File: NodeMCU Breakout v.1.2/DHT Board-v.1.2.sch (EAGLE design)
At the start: 12 parts, among them IC1 74HCT125N

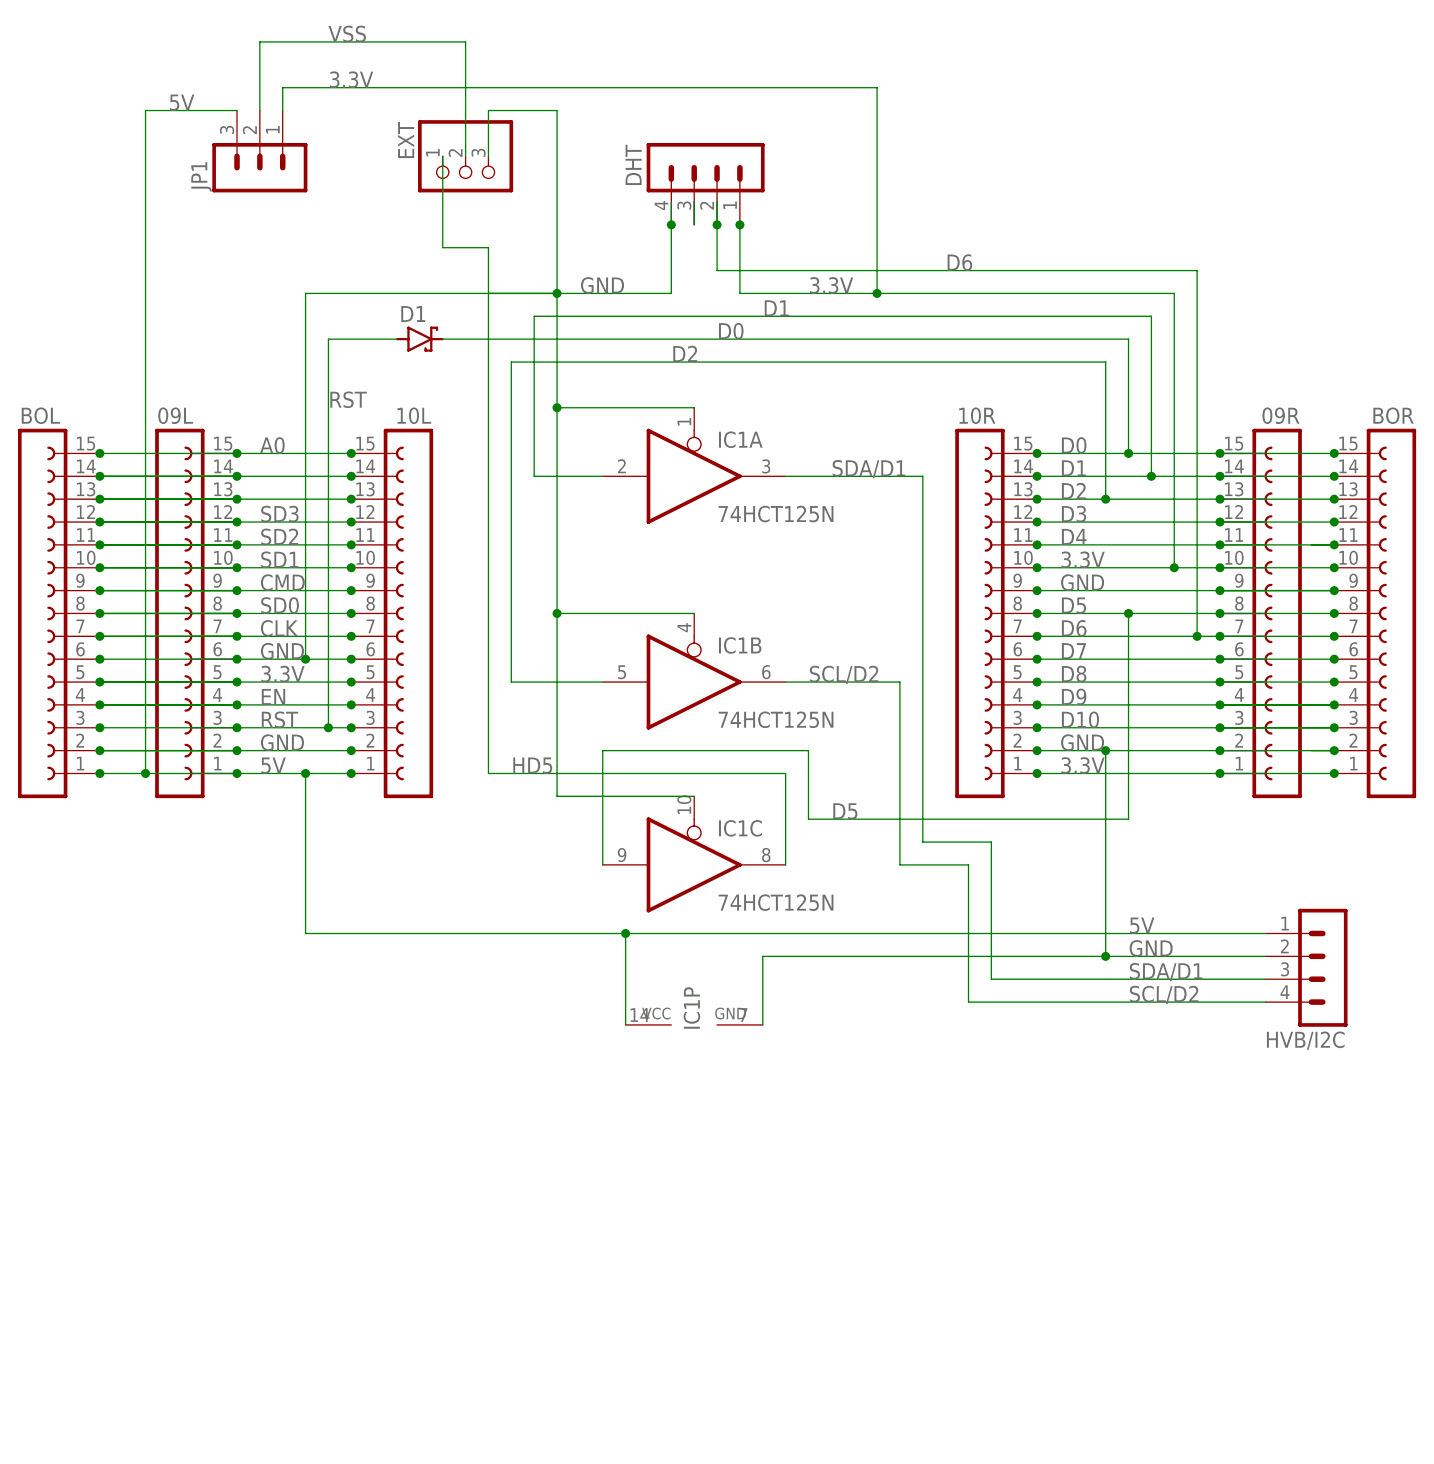
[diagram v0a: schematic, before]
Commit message: 12/26/18(BK): Updated with changes to EXT signal (D4, to make it compatible with all LED drivers), adding another pin to the I2C/HVB header, and adding a set of solder jumpers on the back of the board, for bypassing the level shifter as necessary.
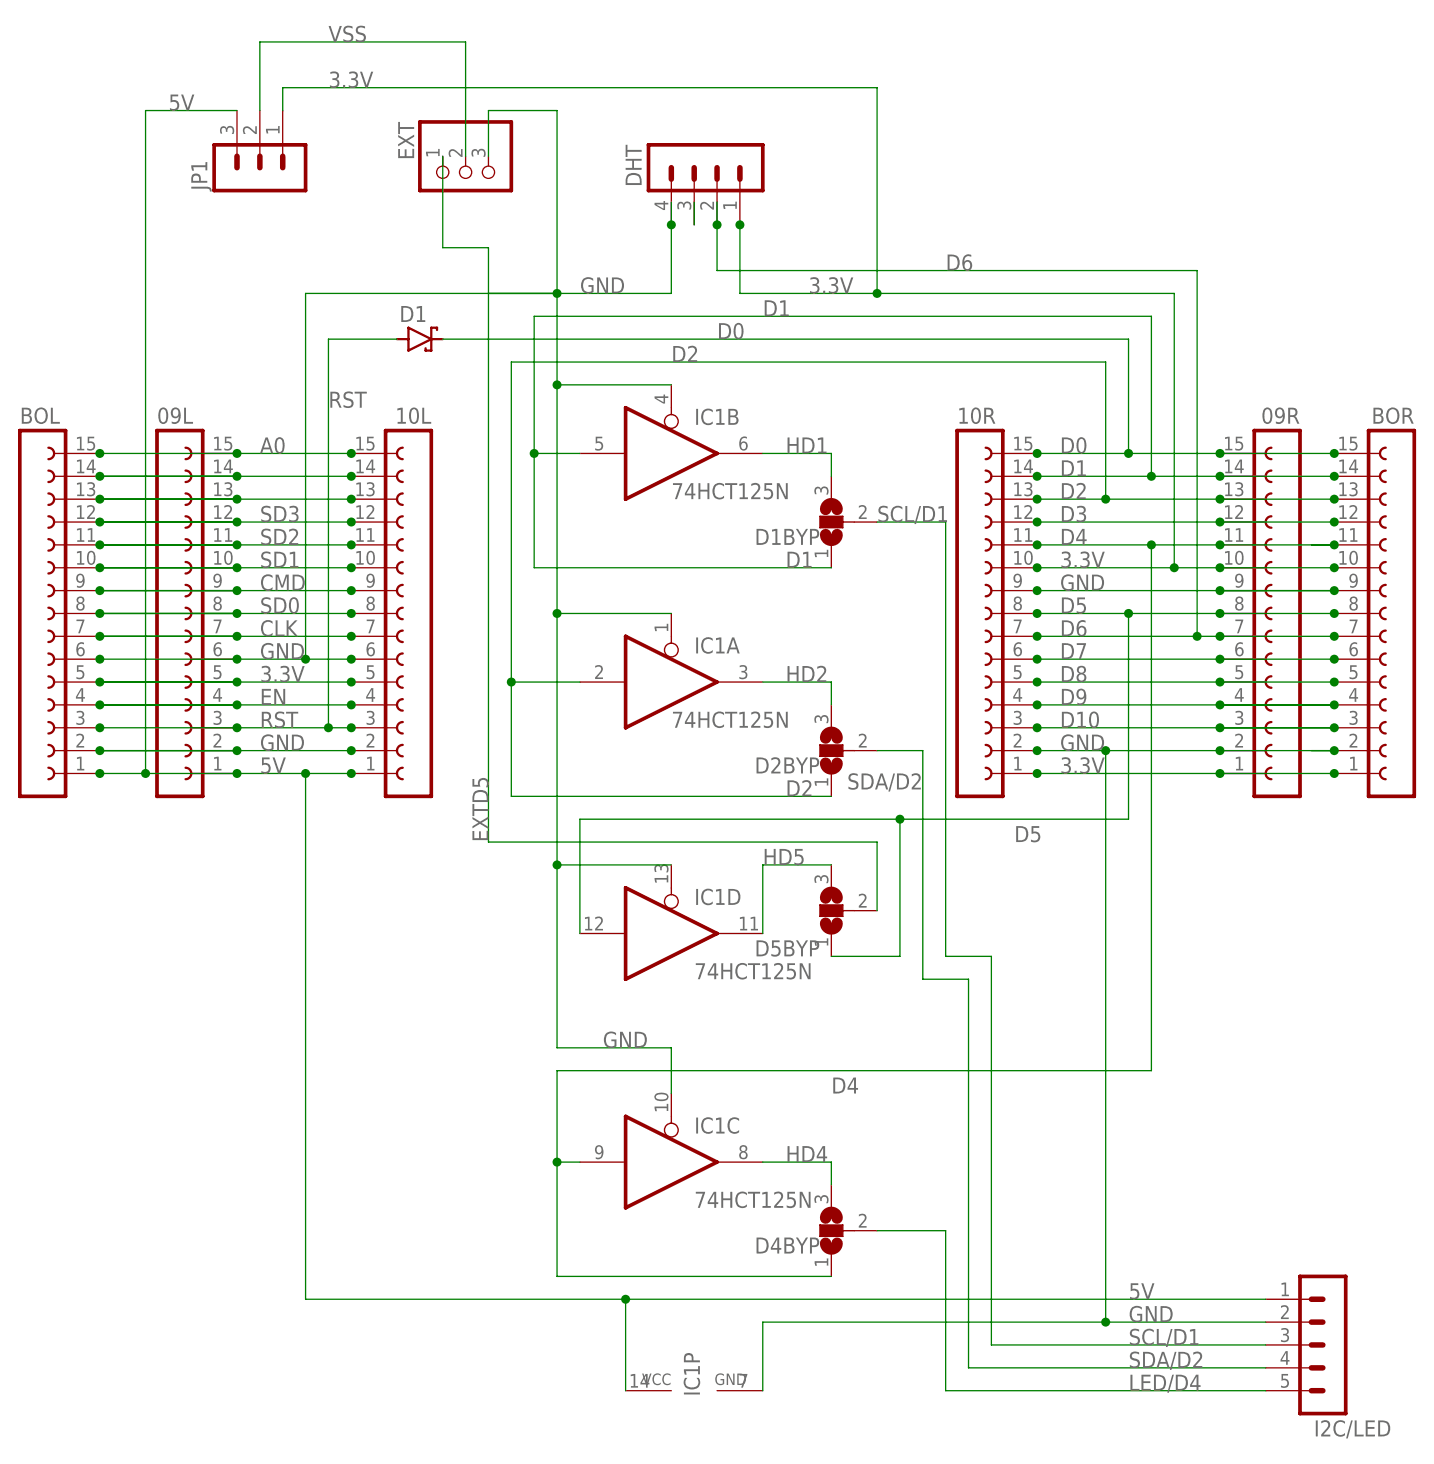
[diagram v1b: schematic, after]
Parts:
- removed HVB/I2C: (no value), con-lstb:MA04-1
- added D1BYP, D2BYP, D4BYP, D5BYP: (no value), jumper:SJ2W
- added I2C/LED: (no value), con-lstb:MA05-1
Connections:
- removed net SCL/D2: HVB/I2C.4, IC1B.O
- removed net SDA/D1: HVB/I2C.3, IC1A.O
- new net EXTD5: D5BYP.2, EXT.1
- new net HD1: D1BYP.3, IC1B.O
- new net HD2: D2BYP.3, IC1A.O
- new net HD4: D4BYP.3, IC1C.O
- new net LED/D4: D4BYP.2, I2C/LED.5
- new net SCL/D1: D1BYP.2, I2C/LED.3
- new net SDA/D2: D2BYP.2, I2C/LED.4
- net 5V: now also I2C/LED.1; no longer HVB/I2C.1
- net D1: now also D1BYP.1, IC1B.I; no longer IC1A.I
- net D2: now also D2BYP.1, IC1A.I; no longer IC1B.I
- net D4: now also D4BYP.1, IC1C.I
- net D5: now also D5BYP.1, IC1D.I; no longer IC1C.I
- net GND: now also I2C/LED.2, IC1D.OE; no longer HVB/I2C.2
- net HD5: now also D5BYP.3, IC1D.O; no longer EXT.1, IC1C.O
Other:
- moved on the sheet: IC1A, IC1B, IC1C, IC1P

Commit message: Updated to add I2C_VCC selector solder bridge (3.3/5v supply) and mounting holes.
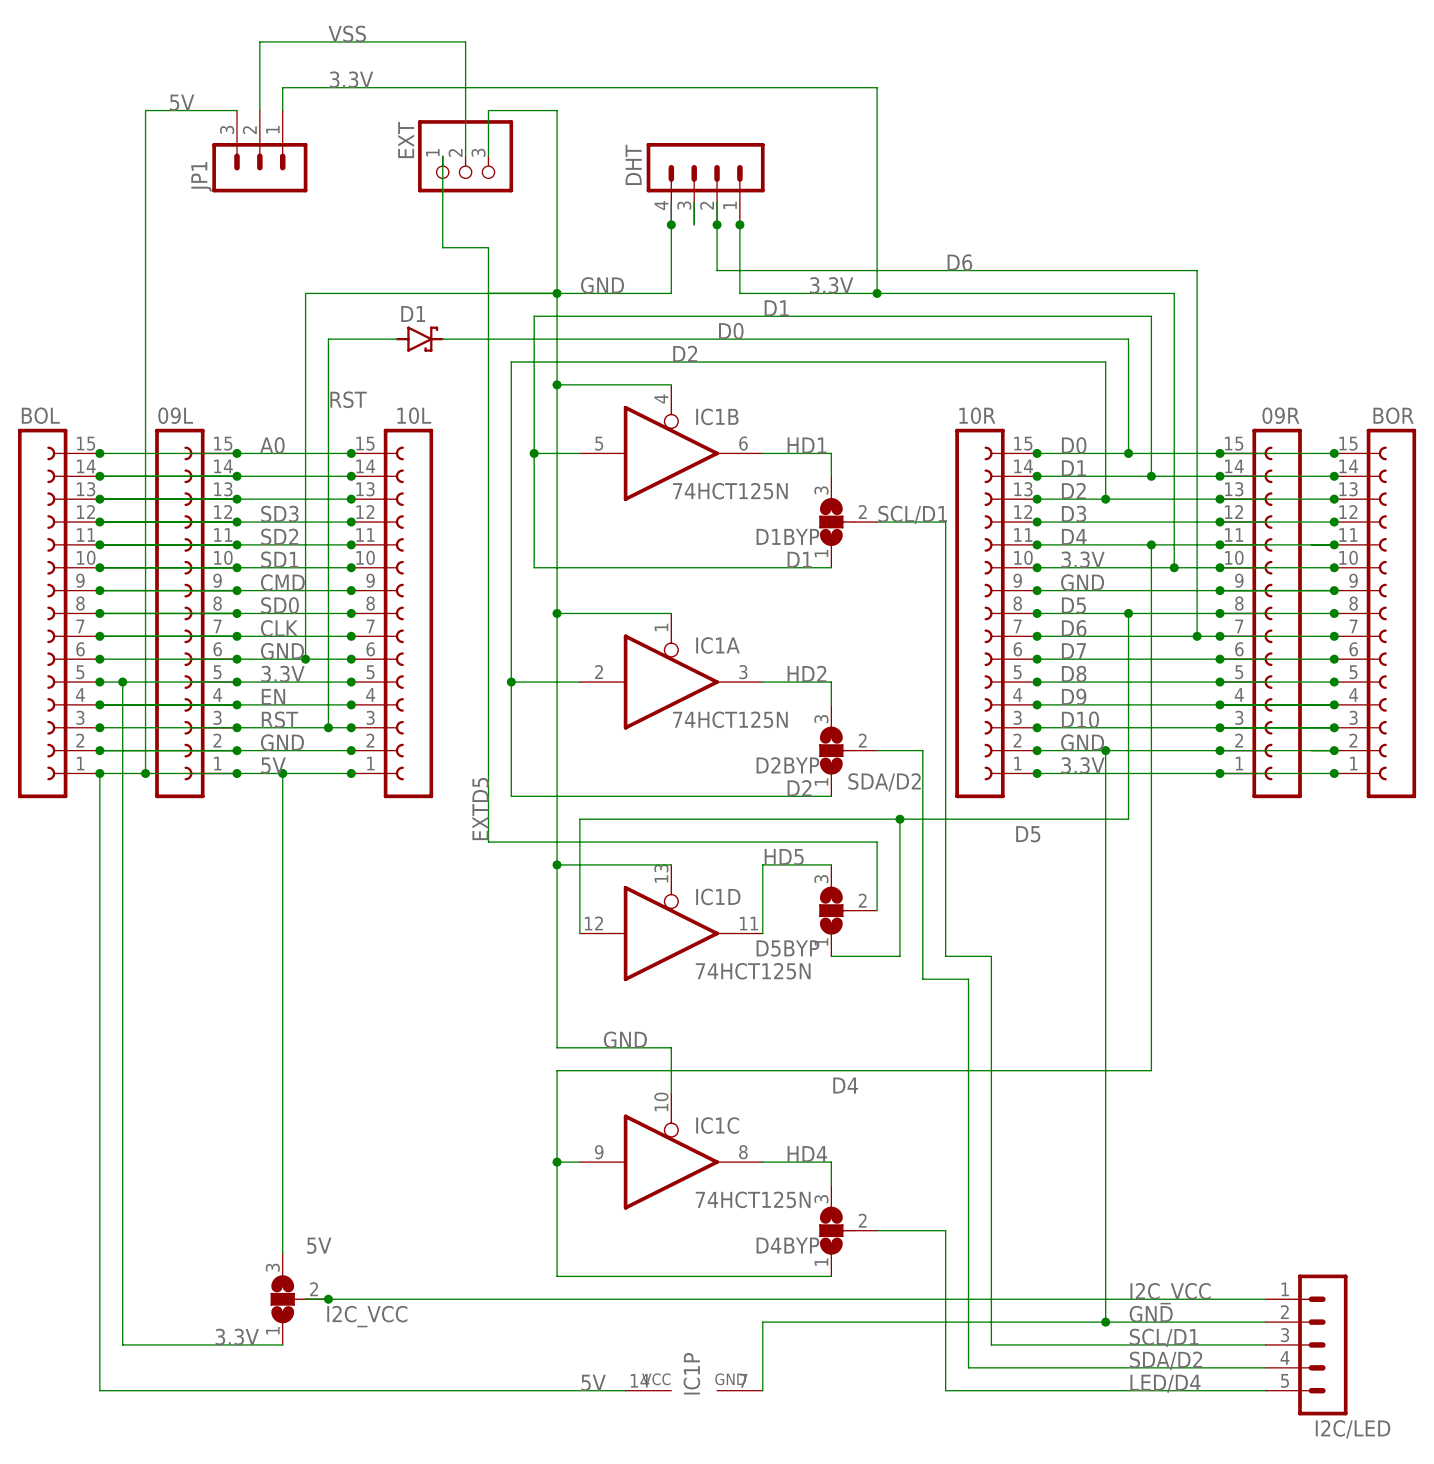
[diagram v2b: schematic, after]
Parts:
- added I2C_VCC: (no value), jumper:SJ2W
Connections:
- new net I2C_VCC: I2C/LED.1, I2C_VCC.2
- net 3.3V: now also I2C_VCC.1
- net 5V: now also I2C_VCC.3; no longer I2C/LED.1
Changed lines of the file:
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@@
 <part name="D2BYP" library="jumper" library_urn="urn:adsk.eagle:library:252" deviceset="SJ2W" device="" package3d_urn="urn:adsk.eagle:package:15474/1"/>
 <part name="D5BYP" library="jumper" library_urn="urn:adsk.eagle:library:252" deviceset="SJ2W" device="" package3d_urn="urn:adsk.eagle:package:15474/1"/>
+<part name="I2C_VCC" library="jumper" library_urn="urn:adsk.eagle:library:252" deviceset="SJ2W" device="" package3d_urn="urn:adsk.eagle:package:15474/1"/>
 </parts>
 <sheets>
@@
 <attribute name="VALUE" x="69.85" y="25.4" size="1.778" layer="96" rot="R180"/>
 <attribute name="NAME" x="67.31" y="14.478" size="1.778" layer="95" rot="R180"/>
+</instance>
+<instance part="I2C_VCC" gate="G$1" x="7.62" y="-25.4" smashed="yes" rot="R180">
+<attribute name="VALUE" x="8.89" y="-17.78" size="1.778" layer="96" rot="R180"/>
+<attribute name="NAME" x="21.59" y="-26.162" size="1.778" layer="95" rot="R180"/>
 </instance>
 </instances>
@@
 </segment>
 </net>
-<net name="5V" class="0">
+<net name="I2C_VCC" class="0">
 <segment>
 <pinref part="I2C/LED" gate="G$1" pin="1"/>
 <label x="101.6" y="-25.4" size="1.778" layer="95"/>
-<pinref part="10L" gate="G$1" pin="1"/>
-<junction x="15.24" y="33.02"/>
-<pinref part="BOL" gate="G$1" pin="1"/>
-<wire x1="2.54" y1="33.02" x2="10.16" y2="33.02" width="0.1524" layer="91"/>
-<junction x="-12.7" y="33.02"/>
-<wire x1="10.16" y1="33.02" x2="15.24" y2="33.02" width="0.1524" layer="91"/>
-<wire x1="-12.7" y1="33.02" x2="-7.62" y2="33.02" width="0.1524" layer="91"/>
-<pinref part="09L" gate="G$1" pin="1"/>
-<junction x="2.54" y="33.02"/>
-<pinref part="JP1" gate="G$1" pin="3"/>
-<wire x1="-7.62" y1="33.02" x2="2.54" y2="33.02" width="0.1524" layer="91"/>
-<wire x1="-7.62" y1="33.02" x2="-7.62" y2="106.68" width="0.1524" layer="91"/>
-<wire x1="-7.62" y1="106.68" x2="2.54" y2="106.68" width="0.1524" layer="91"/>
-<junction x="-7.62" y="33.02"/>
-<label x="5.08" y="33.02" size="1.778" layer="95"/>
-<label x="-5.08" y="106.68" size="1.778" layer="95"/>
-<wire x1="10.16" y1="33.02" x2="10.16" y2="-25.4" width="0.1524" layer="91"/>
-<junction x="10.16" y="33.02"/>
-<wire x1="116.84" y1="-25.4" x2="45.72" y2="-25.4" width="0.1524" layer="91"/>
-<wire x1="45.72" y1="-25.4" x2="10.16" y2="-25.4" width="0.1524" layer="91"/>
-<wire x1="45.72" y1="-35.56" x2="45.72" y2="-25.4" width="0.1524" layer="91"/>
-<junction x="45.72" y="-25.4"/>
-<pinref part="IC1" gate="P" pin="VCC"/>
+<wire x1="116.84" y1="-25.4" x2="12.7" y2="-25.4" width="0.1524" layer="91"/>
+<wire x1="12.7" y1="-25.4" x2="10.16" y2="-25.4" width="0.1524" layer="91"/>
+<pinref part="I2C_VCC" gate="G$1" pin="2"/>
+<junction x="12.7" y="-25.4"/>
 </segment>
 </net>
@@
 <junction x="15.24" y="43.18"/>
 <pinref part="BOL" gate="G$1" pin="5"/>
-<wire x1="-12.7" y1="43.18" x2="2.54" y2="43.18" width="0.1524" layer="91"/>
 <junction x="-12.7" y="43.18"/>
 <wire x1="2.54" y1="43.18" x2="15.24" y2="43.18" width="0.1524" layer="91"/>
-<wire x1="-12.7" y1="43.18" x2="2.54" y2="43.18" width="0.1524" layer="91"/>
+<wire x1="-12.7" y1="43.18" x2="-10.16" y2="43.18" width="0.1524" layer="91"/>
 <pinref part="09L" gate="G$1" pin="5"/>
 <junction x="2.54" y="43.18"/>
 <label x="5.08" y="43.18" size="1.778" layer="95"/>
+<wire x1="-10.16" y1="43.18" x2="2.54" y2="43.18" width="0.1524" layer="91"/>
+<wire x1="-10.16" y1="43.18" x2="-10.16" y2="-30.48" width="0.1524" layer="91"/>
+<junction x="-10.16" y="43.18"/>
+<pinref part="I2C_VCC" gate="G$1" pin="1"/>
+<wire x1="-10.16" y1="-30.48" x2="7.62" y2="-30.48" width="0.1524" layer="91"/>
+<label x="0" y="-30.48" size="1.778" layer="95"/>
 </segment>
 </net>
@@
 </segment>
 </net>
+<net name="5V" class="0">
+<segment>
+<pinref part="JP1" gate="G$1" pin="3"/>
+<wire x1="-7.62" y1="106.68" x2="2.54" y2="106.68" width="0.1524" layer="91"/>
+<pinref part="10L" gate="G$1" pin="1"/>
+<junction x="15.24" y="33.02"/>
+<wire x1="2.54" y1="33.02" x2="7.62" y2="33.02" width="0.1524" layer="91"/>
+<pinref part="09L" gate="G$1" pin="1"/>
+<junction x="2.54" y="33.02"/>
+<wire x1="7.62" y1="33.02" x2="15.24" y2="33.02" width="0.1524" layer="91"/>
+<wire x1="-7.62" y1="33.02" x2="2.54" y2="33.02" width="0.1524" layer="91"/>
+<wire x1="-7.62" y1="33.02" x2="-7.62" y2="106.68" width="0.1524" layer="91"/>
+<junction x="-7.62" y="33.02"/>
+<pinref part="BOL" gate="G$1" pin="1"/>
+<junction x="-12.7" y="33.02"/>
+<wire x1="-12.7" y1="33.02" x2="-7.62" y2="33.02" width="0.1524" layer="91"/>
+<label x="5.08" y="33.02" size="1.778" layer="95"/>
+<label x="-5.08" y="106.68" size="1.778" layer="95"/>
+<pinref part="I2C_VCC" gate="G$1" pin="3"/>
+<wire x1="7.62" y1="-20.32" x2="7.62" y2="33.02" width="0.1524" layer="91"/>
+<junction x="7.62" y="33.02"/>
+<label x="10.16" y="-20.32" size="1.778" layer="95"/>
+<wire x1="-12.7" y1="33.02" x2="-12.7" y2="-35.56" width="0.1524" layer="91"/>
+<pinref part="IC1" gate="P" pin="VCC"/>
+<wire x1="-12.7" y1="-35.56" x2="45.72" y2="-35.56" width="0.1524" layer="91"/>
+<label x="40.64" y="-35.56" size="1.778" layer="95"/>
+</segment>
+</net>
